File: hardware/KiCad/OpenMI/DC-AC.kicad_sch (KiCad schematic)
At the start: 41 parts, among them Q2 IPL60R125P7, Q3 IPL60R125P7, U1 IRS2304S

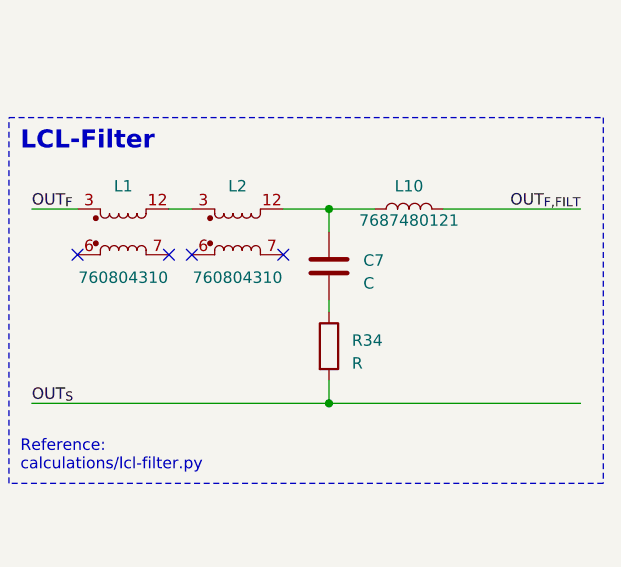
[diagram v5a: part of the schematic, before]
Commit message: feat(hw): Adds filter capacitor.
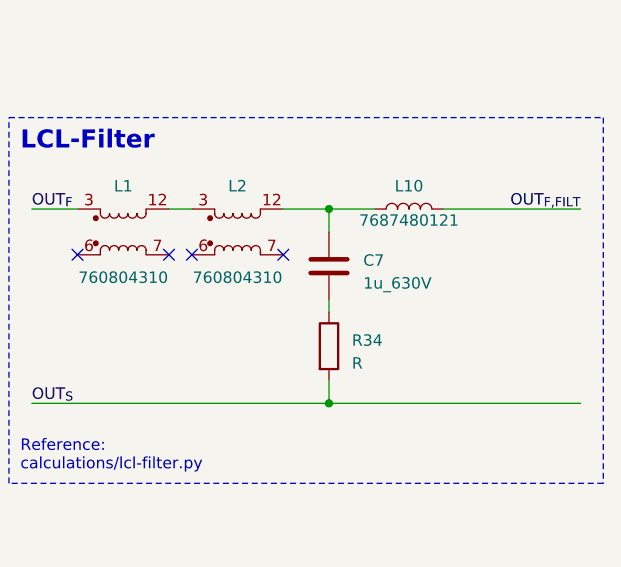
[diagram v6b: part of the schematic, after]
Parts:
- removed C7: C, symbol Device:C
- added C7: 1u_630V, Capacitor_THT:C_Rect_L26.5mm_W8.5mm_P22.50mm_MKS4, symbol _C_Film:1u_630V
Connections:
- net at R34.1: now also C7.2
- net at L10.1, L2.12: now also C7.1
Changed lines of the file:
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@@
+    )
+  )
+  (symbol (lib_id "_C_Film:1u_630V") (at 199.39 101.6 0) (unit 1)
+    (in_bom yes) (on_board yes) (dnp no) (fields_autoplaced)
+    (property "Reference" "C7" (at 203.2 100.965 0)
+      (effects (font (size 1.27 1.27)) (justify left))
+    )
+    (property "Value" "1u_630V" (at 203.2 103.505 0)
+      (effects (font (size 1.27 1.27)) (justify left))
+    )
+    (property "Footprint" "Capacitor_THT:C_Rect_L26.5mm_W8.5mm_P22.50mm_MKS4" (at 200.3552 105.41 0)
+      (effects (font (size 1.27 1.27)) hide)
+    )
+    (property "Datasheet" "https://www.mouser.de/datasheet/2/315/ABD0000C255-1131244.pdf" (at 199.39 101.6 0)
+      (effects (font (size 1.27 1.27)) hide)
+    )
+    (property "MF" "Panasonic" (at 199.39 101.6 0)
+      (effects (font (size 1.27 1.27)) hide)
+    )
+    (property "MPN" "ECW-FD2J105J" (at 199.39 101.6 0)
+      (effects (font (size 1.27 1.27)) hide)
+    )
+    (property "OC_CONRAD" "" (at 199.39 101.6 0)
+      (effects (font (size 1.27 1.27)) hide)
+    )
+    (property "OC_FARNELL" "" (at 199.39 101.6 0)
+      (effects (font (size 1.27 1.27)) hide)
+    )
+    (property "OC_LCSC" "" (at 199.39 101.6 0)
+      (effects (font (size 1.27 1.27)) hide)
+    )
+    (property "OC_MOUSER" "667-ECW-FD2J105J" (at 199.39 101.6 0)
+      (effects (font (size 1.27 1.27)) hide)
+    )
+    (property "OC_REICHELT" "" (at 199.39 101.6 0)
+      (effects (font (size 1.27 1.27)) hide)
+    )
+    (pin "1")
+    (pin "2")
+    (instances
+      (project "OpenMI"
+        (path "/2d959e19-1572-42a0-a8fd-da8463ad4e66/19323a41-9b99-4de4-bfae-f2f828815be3"
+          (reference "C7") (unit 1)
+        )
+      )
     )
   )
@@
         )
       )
-    )
-  )
-  (symbol (lib_id "Device:C") (at 199.39 101.6 0) (unit 1)
-    (in_bom yes) (on_board yes) (dnp no) (fields_autoplaced)
-    (property "Reference" "C7" (at 203.2 100.965 0)
-      (effects (font (size 1.27 1.27)) (justify left))
-    )
-    (property "Value" "C" (at 203.2 103.505 0)
-      (effects (font (size 1.27 1.27)) (justify left))
-    )
-    (property "Footprint" "" (at 200.3552 105.41 0)
-      (effects (font (size 1.27 1.27)) hide)
-    )
-    (property "Datasheet" "~" (at 199.39 101.6 0)
-      (effects (font (size 1.27 1.27)) hide)
-    )
-    (pin "1")
-    (pin "2")
-    (instances
-      (project "OpenMI"
-        (path "/2d959e19-1572-42a0-a8fd-da8463ad4e66/19323a41-9b99-4de4-bfae-f2f828815be3"
-          (reference "C7") (unit 1)
-        )
-      )

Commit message: docs(hw): Updates symbol from library
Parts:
- L1, L2: MF Wurth Elektronik -> Wuerth Elektronik
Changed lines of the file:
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@@
       (effects (font (size 1.27 1.27)) hide)
     )
-    (property "MF" "Wurth Elektronik" (at 189.23 97.79 0)
+    (property "MF" "Wuerth Elektronik" (at 189.23 97.79 0)
       (effects (font (size 1.27 1.27)) hide)
     )
@@
       (effects (font (size 1.27 1.27)) hide)
     )
-    (property "MF" "Wurth Elektronik" (at 176.53 97.79 0)
+    (property "MF" "Wuerth Elektronik" (at 176.53 97.79 0)
       (effects (font (size 1.27 1.27)) hide)
     )

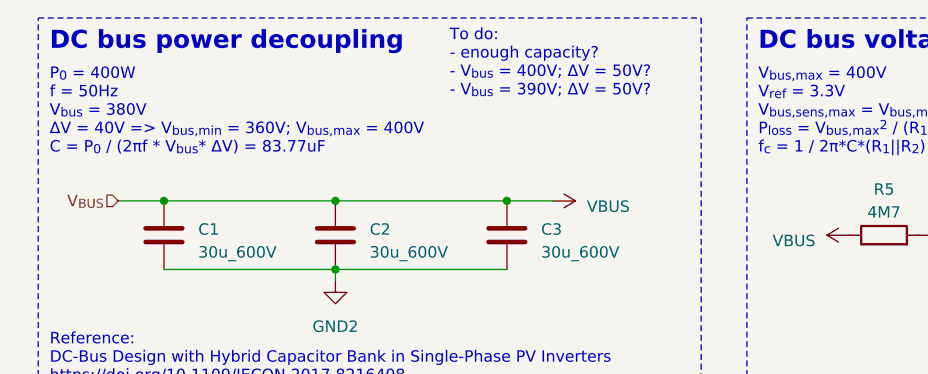
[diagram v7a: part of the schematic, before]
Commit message: docs(hw): updates DC bus power decoupling calculation
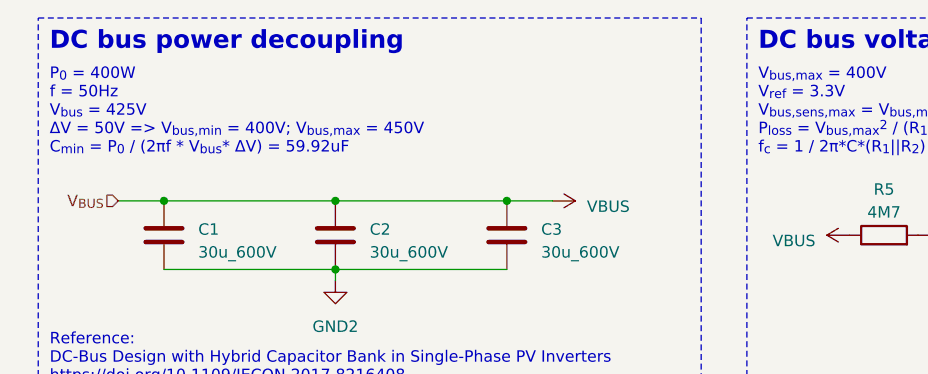
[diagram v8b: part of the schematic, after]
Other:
- note added: "P_{0} = 400W f = 50Hz V_{bus} = 425V ΔV = 50V => V_{bus,min} = 400V; V_{bus,max} = 450V C_{min} = P_{0} / (2πf * V_{bus}* ΔV) = 59.92uF"
- note removed: "P_{0} = 400W f = 50Hz V_{bus} = 380V ΔV = 40V => V_{bus,min} = 360V; V_{bus,max} = 400V C = P_{0} / (2πf * V_{bus}* ΔV) = 83.77uF"
- note removed: "To do: - enough capacity? - V_{bus} = 400V; ΔV = 50V? - V_{bus} = 390V; ΔV = 50V?"
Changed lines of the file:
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@@
     (effects (font (size 2 2) (thickness 0.4) bold) (justify left bottom))
   )
-  (text "P_{0} = 400W\nf = 50Hz\nV_{bus} = 380V\nΔV = 40V => V_{bus,min} = 360V; V_{bus,max} = 400V\nC = P_{0} / (2πf * V_{bus}* ΔV) = 83.77uF"
+  (text "P_{0} = 400W\nf = 50Hz\nV_{bus} = 425V\nΔV = 50V => V_{bus,min} = 400V; V_{bus,max} = 450V\nC_{min} = P_{0} / (2πf * V_{bus}* ΔV) = 59.92uF"
     (at 17.78 31.75 0)
     (effects (font (size 1.27 1.27)) (justify left bottom))
@@
     (effects (font (size 2 2) bold) (justify left bottom))
   )
-  (text "To do:\n- enough capacity?\n- V_{bus} = 400V; ΔV = 50V?\n- V_{bus} = 390V; ΔV = 50V?"
-    (at 62.23 25.4 0)
-    (effects (font (size 1.27 1.27)) (justify left bottom))
-  )
   (text "Reference: \ncalculations/lcl-filter.py" (at 165.1 124.46 0)
